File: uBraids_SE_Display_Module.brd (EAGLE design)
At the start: 40 x 25 mm, 40 parts, among them Q1 NPN-SOT323-BEC, Q2 NPN-SOT323-BEC, Q3 NPN-SOT323-BEC, Q4 NPN-SOT323-BEC, U1 SN74HC595-TSSOP-16, U2 SN74HC595-TSSOP-16

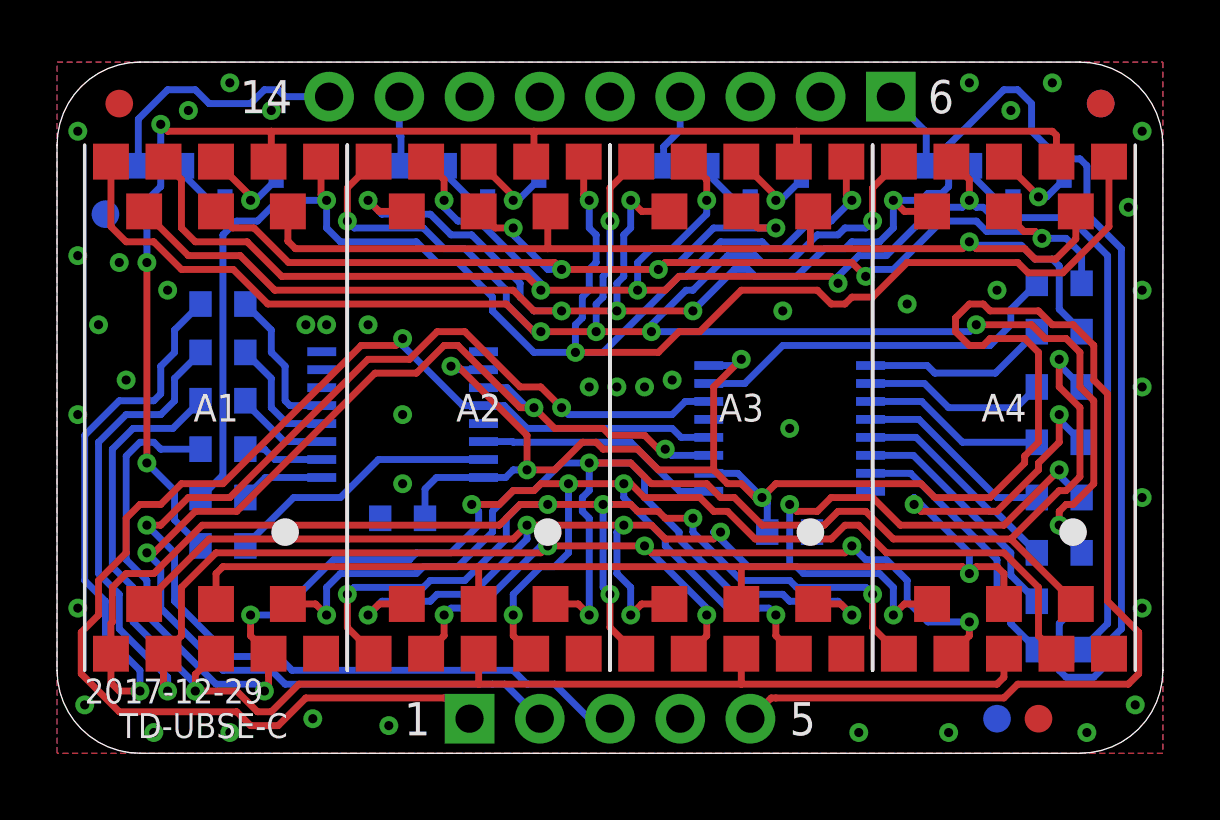
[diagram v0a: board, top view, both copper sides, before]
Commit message: update for Revision E production
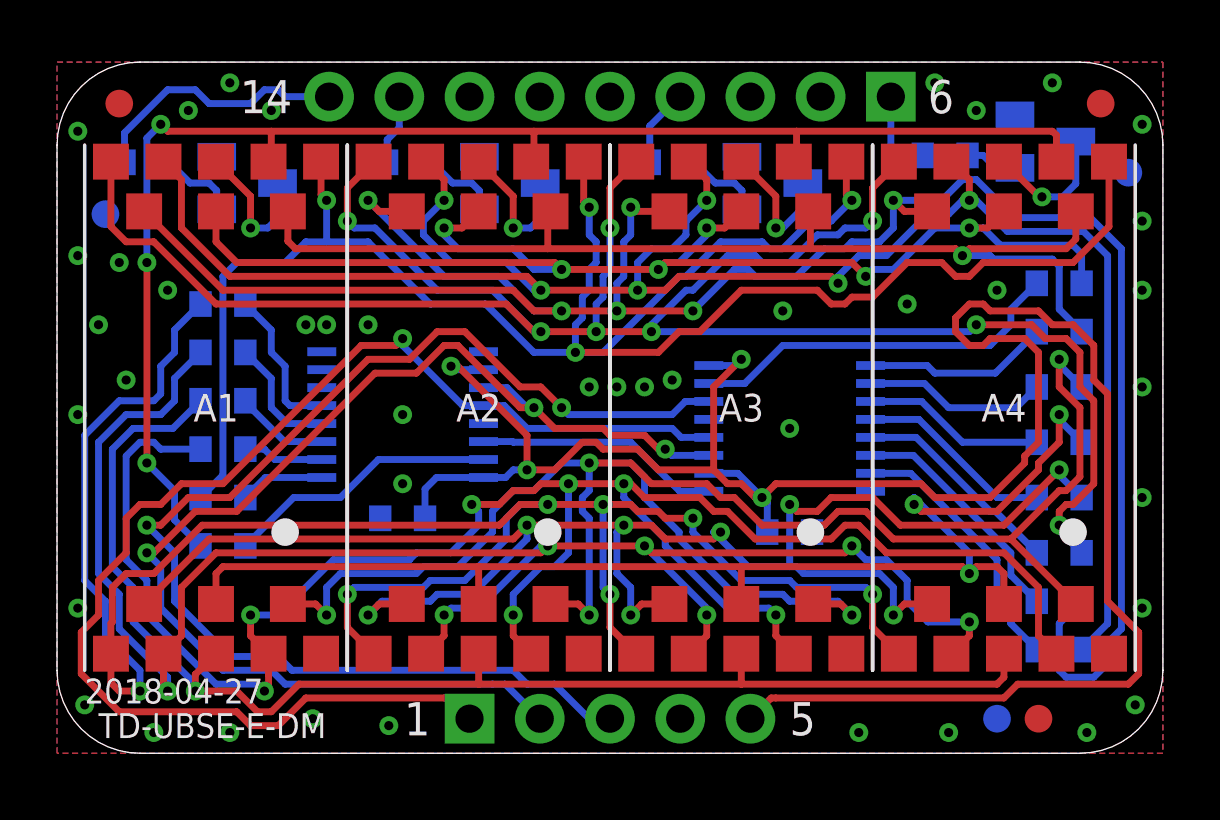
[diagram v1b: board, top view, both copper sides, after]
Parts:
- removed U$9: (no value), uBraids_SE:MARKING-OSH-LOGO-5MM
- added U$7: (no value), uBraids_SE_Library:MARKING-CC-LOGO
- A1, A2, A3, A4: device uBraids_SE:14-SEGMENT-0.4"-SMD -> uBraids_SE_Library:14-SEGMENT-0.4"-SMD
- C1, C2, R1, R10, R11, R12, R13, R14, R15, R16, R17, R18, R2, R3, R4, R5, R6, R7, R8, R9: device uBraids_SE:0603-NP -> uBraids_SE_Library:0603-NP
- H1: device Headers:HEADER-1X05-PTH-2.54-MALE -> uBraids_SE_Library:HEADER-1X05-PTH-2.54-MALE
- H2: device Headers:HEADER-1X09-PTH-2.54-MALE -> uBraids_SE_Library:HEADER-1X09-PTH-2.54-MALE
- Q1, Q2, Q3, Q4: value NPN-SOT323-BEC -> NPN-SOT23-BEC; device uBraids_SE:SOT-323 -> uBraids_SE_Library:SOT-23
- U$1, U$2, U$3, U$4, U$5, U$6: device uBraids_SE:FIDUCIAL -> uBraids_SE_Library:FIDUCIAL
- U$8: device uBraids_SE:MARKING-CC-LOGO -> uBraids_SE_Library:MARKING-OSH-LOGO-5MM
- U1, U2: device uBraids_SE:TSSOP-16 -> uBraids_SE_Library:TSSOP-16
- moved U$3 40.0 mm to (2.25, 23.5)
- moved U$1 35.5 mm to (37.8, 23.5)
- moved U$2 22.4 mm to (35.5, 1.25)
- moved U$8 11.7 mm to (10.5, 17.0)
- moved U$5 2.69 mm to (38.8, 21.0)
- moved Q4 1.40 mm to (35.8, 22.1), turned to 90 degrees
- moved R1 0.52 mm to (3.25, 21.4)
- moved R2 0.52 mm to (12.8, 21.4)
- moved R3 0.52 mm to (22.2, 21.4)
- moved R4 0.40 mm to (32.1, 21.6)
- moved Q1 0.18 mm to (6.88, 20.6), turned to 90 degrees
- moved Q2 0.18 mm to (16.4, 20.6), turned to 90 degrees
- moved Q3 0.18 mm to (25.9, 20.6), turned to 90 degrees
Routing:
- net G: track 83.8 -> 77.9 mm
- net A2C: track 3.15 -> 5.31 mm
- net A1C: track 3.15 -> 5.31 mm
- net A3C: track 3.15 -> 5.09 mm
- net A4C: track 2.98 -> 4.85 mm
- net H: track 69.1 -> 70.6 mm
- net K: track 73.4 -> 72.0 mm
- net Q2B: track 2.17 -> 2.81 mm
- net Q1B: track 2.17 -> 2.81 mm
- net Q3B: track 2.17 -> 2.81 mm
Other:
- board text added: "2018-04-27"
- board text added: "TD-UBSE-E-DM"
- board text added: "TD-UBSE-E-DM 2018-04-27 tall-dog.com"
- board text removed: "2017-12-29"
- board text removed: "TALL-DOG.COM 2017-12-29 TD-UBSE-C"
- board text removed: "TD-UBSE-C"

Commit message: Revision F
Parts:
- removed U$7: (no value), uBraids_SE_Library:MARKING-CC-LOGO
- removed U$8: (no value), uBraids_SE_Library:MARKING-OSH-LOGO-5MM
- A1, A2, A3, A4: device uBraids_SE_Library:14-SEGMENT-0.4"-SMD -> uBraids_SE_Library:14-SEGMENT
- H1: value HEADER-1X05-PTH-2.54-MALE -> HEADER-1X5-PTH; device uBraids_SE_Library:HEADER-1X05-PTH-2.54-MALE -> uBraids_SE_Library:PTH-0.1-1X5
- H2: value HEADER-1X09-PTH-2.54-MALE -> HEADER-1X9-PTH; device uBraids_SE_Library:HEADER-1X09-PTH-2.54-MALE -> uBraids_SE_Library:PTH-0.1-1X9
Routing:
- net N: track 64.8 -> 63.5 mm
- net L: track 71.3 -> 70.5 mm
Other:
- board text added: "C1"
- board text added: "C2"
- board text added: "C3"
- board text added: "C4"
- board text added: "TD-UBSE-F-DM 2020-02-07 tall-dog.com"
- board text removed: "2018-04-27"
- board text removed: "DC1"
- board text removed: "DC2"
- board text removed: "DC3"
- board text removed: "DC4"
- board text removed: "H1"
- board text removed: "H2"
- board text removed: "TD-UBSE-E-DM"
- board text removed: "TD-UBSE-E-DM 2018-04-27 tall-dog.com"
